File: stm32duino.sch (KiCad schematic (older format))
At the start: 19 parts, among them P1 RF7021SE, P2 DISP_I2C, P3 DISP_SER, P4 HOST_SER, U1 stm32f103c8t6-module-china

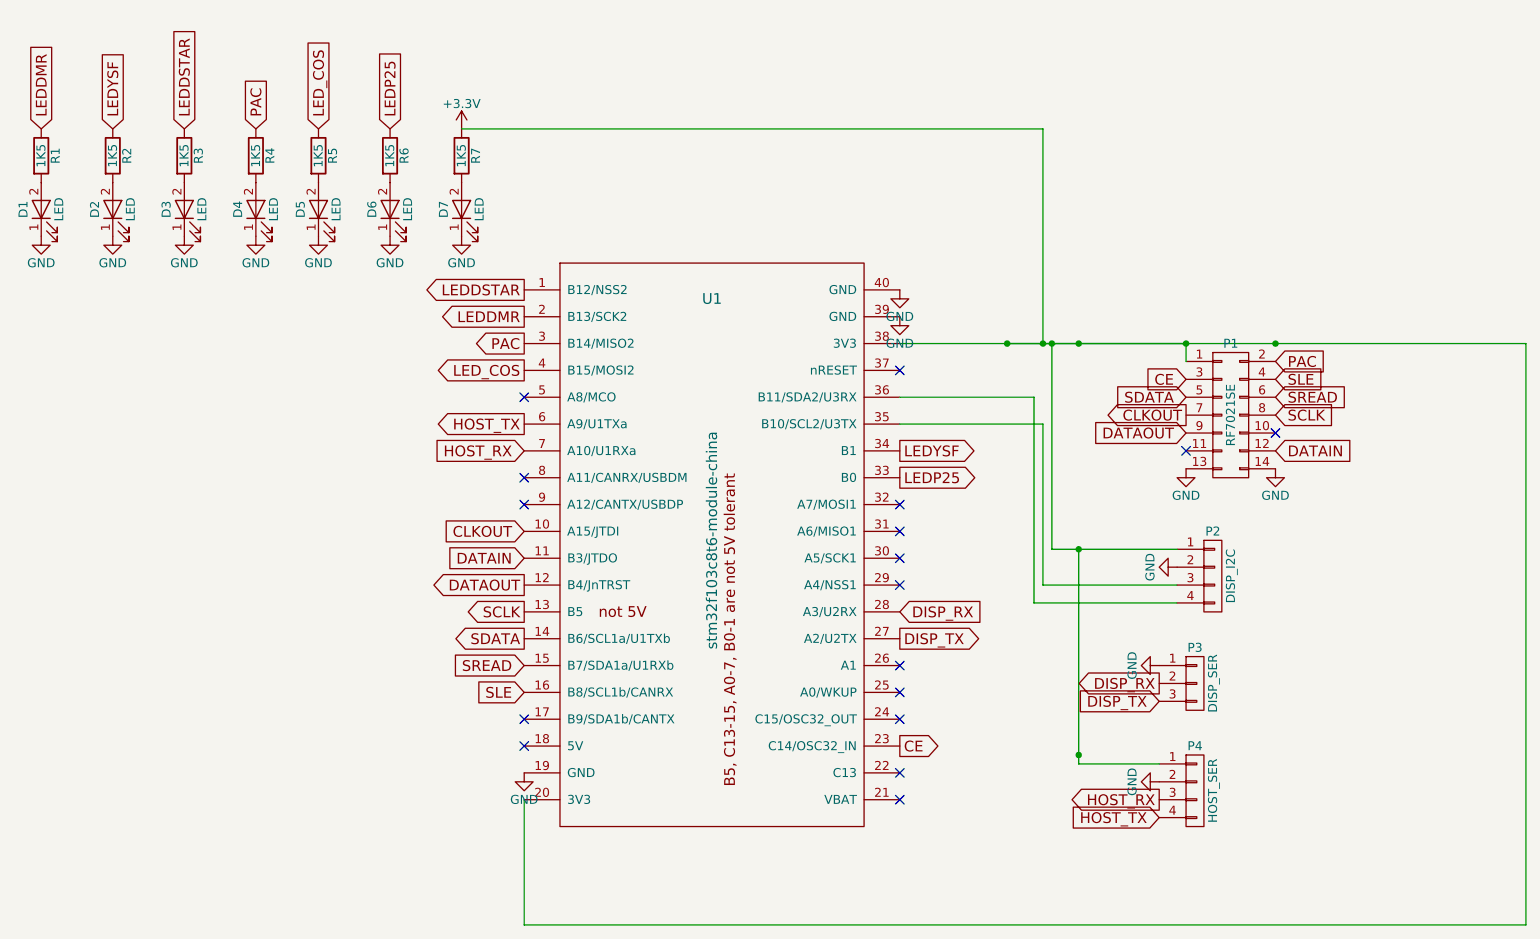
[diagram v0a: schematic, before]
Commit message: Minor beautification, added OSHW logo to PCB
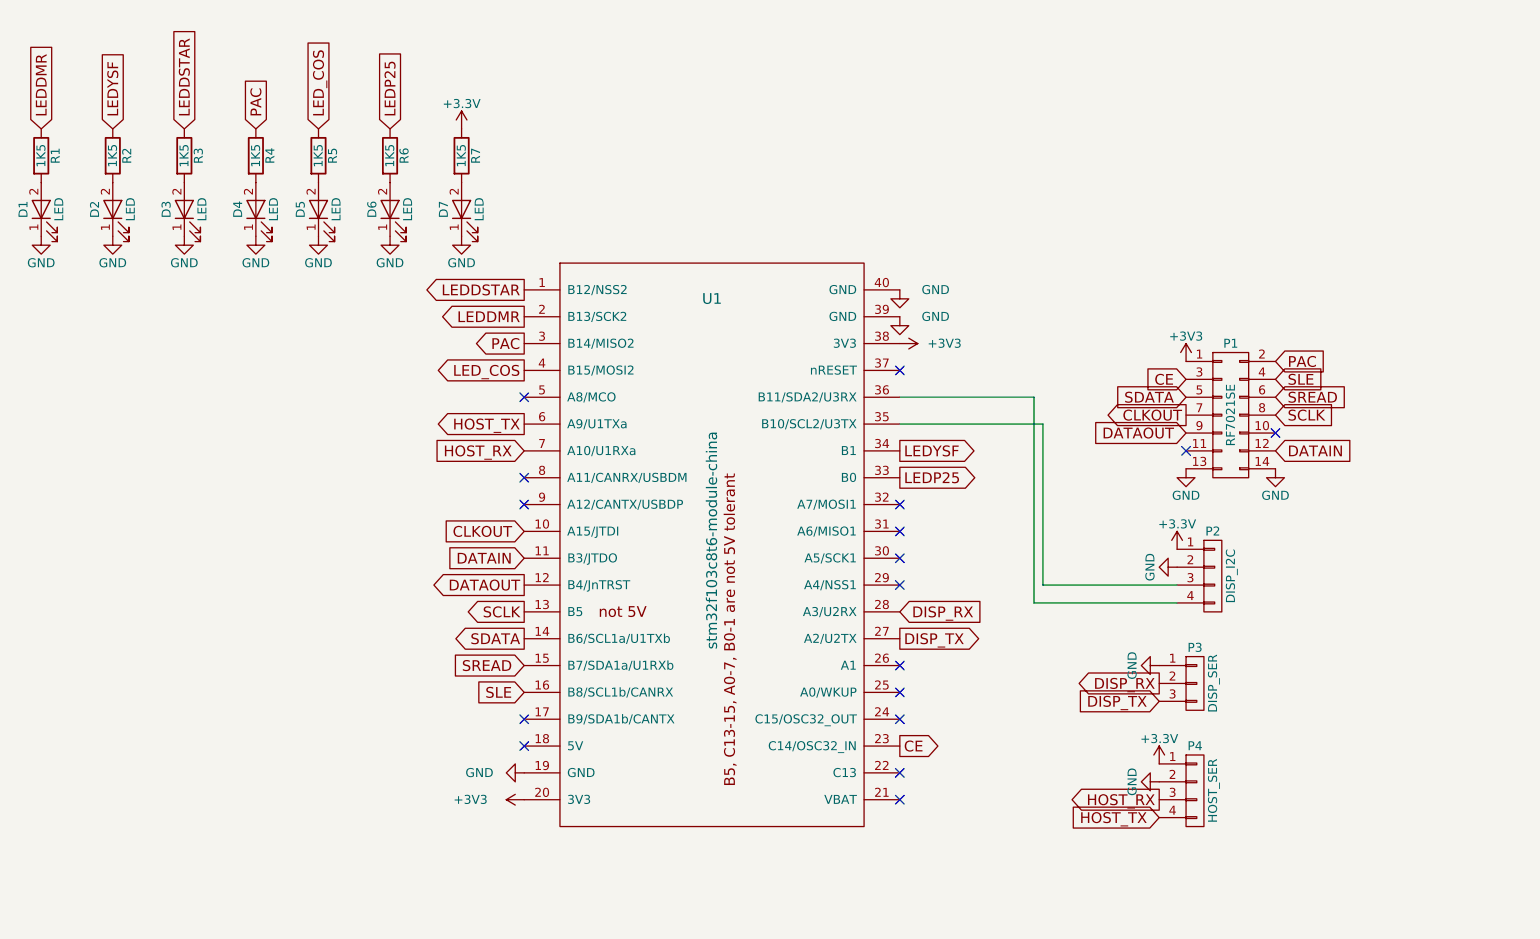
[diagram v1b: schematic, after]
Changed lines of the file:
@@
 P 6200 1900
 F 0 "#PWR10" H 6200 1650 50  0001 C CNN
-F 1 "GND" H 6200 1750 50  0000 C CNN
+F 1 "GND" H 6400 1900 50  0000 C CNN
 F 2 "" H 6200 1900 50  0000 C CNN
 F 3 "" H 6200 1900 50  0000 C CNN
@@
 P 6200 2050
 F 0 "#PWR11" H 6200 1800 50  0001 C CNN
-F 1 "GND" H 6200 1900 50  0000 C CNN
+F 1 "GND" H 6400 2050 50  0000 C CNN
 F 2 "" H 6200 2050 50  0000 C CNN
 F 3 "" H 6200 2050 50  0000 C CNN
@@
 P 4100 4600
 F 0 "#PWR9" H 4100 4350 50  0001 C CNN
-F 1 "GND" H 4100 4450 50  0000 C CNN
+F 1 "GND" V 4100 4350 50  0000 C CNN
 F 2 "" H 4100 4600 50  0000 C CNN
 F 3 "" H 4100 4600 50  0000 C CNN
 	1    4100 4600
-	1    0    0    -1
-$EndComp
-Wire Wire Line
-	6200 2200 9700 2200
-Wire Wire Line
-	3750 1000 7000 1000
-Wire Wire Line
-	7000 1000 7000 2200
-Connection ~ 7000 2200
-Wire Wire Line
-	6800 2200 7800 2200
-Wire Wire Line
-	9700 2200 9700 5450
-Wire Wire Line
-	9700 5450 4100 5450
-Connection ~ 6800 2200
-Wire Wire Line
-	4100 5450 4100 4750
-Connection ~ 8300 2200
-Wire Wire Line
-	7800 2200 7800 2300
-Connection ~ 7800 2200
+	0    1    1    0
+$EndComp
 $Comp
 L CONN_01X04 P2
@@
 $EndComp
 Wire Wire Line
-	7050 2200 7050 3350
-Wire Wire Line
-	7050 3350 7750 3350
-Connection ~ 7050 2200
-Wire Wire Line
 	6200 2650 7000 2650
-Wire Wire Line
-	7000 2650 7000 3550
-Wire Wire Line
-	7000 3550 7750 3550
 Wire Wire Line
 	6200 2500 6950 2500
@@
 	1    0    0    -1
 $EndComp
-Connection ~ 7200 2200
-Wire Wire Line
-	7200 4550 7650 4550
-Wire Wire Line
-	7200 3350 7200 4550
-Connection ~ 7200 4500
-Connection ~ 7200 3350
 Text GLabel 4100 2800 0    60   Input ~ 0
 HOST_RX
@@
 Text GLabel 7650 4200 0    60   Input ~ 0
 DISP_TX
+$Comp
+L +3V3 #PWR?
+U 1 1 58E0F416
+P 7800 2300
+F 0 "#PWR?" H 7800 2150 50  0001 C CNN
+F 1 "+3V3" H 7800 2440 50  0000 C CNN
+F 2 "" H 7800 2300 50  0000 C CNN
+F 3 "" H 7800 2300 50  0000 C CNN
+	1    7800 2300
+	1    0    0    -1
+$EndComp
+$Comp
+L +3V3 #PWR?
+U 1 1 58E0F536
+P 4100 4750
+F 0 "#PWR?" H 4100 4600 50  0001 C CNN
+F 1 "+3V3" V 4100 5050 50  0000 C CNN
+F 2 "" H 4100 4750 50  0000 C CNN
+F 3 "" H 4100 4750 50  0000 C CNN
+	1    4100 4750
+	0    -1   -1   0
+$EndComp
+$Comp
+L +3.3V #PWR?
+U 1 1 58E10142
+P 7750 3350
+F 0 "#PWR?" H 7750 3200 50  0001 C CNN
+F 1 "+3.3V" H 7750 3490 50  0000 C CNN
+F 2 "" H 7750 3350 50  0000 C CNN
+F 3 "" H 7750 3350 50  0000 C CNN
+	1    7750 3350
+	1    0    0    -1
+$EndComp
+Wire Wire Line
+	7000 3550 7750 3550
+Wire Wire Line
+	7000 2650 7000 3550
+$Comp
+L +3.3V #PWR?
+U 1 1 58E117A0
+P 7650 4550
+F 0 "#PWR?" H 7650 4400 50  0001 C CNN
+F 1 "+3.3V" H 7650 4690 50  0000 C CNN
+F 2 "" H 7650 4550 50  0000 C CNN
+F 3 "" H 7650 4550 50  0000 C CNN
+	1    7650 4550
+	1    0    0    -1
+$EndComp
+$Comp
+L +3V3 #PWR?
+U 1 1 58E13D3E
+P 6200 2200
+F 0 "#PWR?" H 6200 2050 50  0001 C CNN
+F 1 "+3V3" V 6200 2450 50  0000 C CNN
+F 2 "" H 6200 2200 50  0000 C CNN
+F 3 "" H 6200 2200 50  0000 C CNN
+	1    6200 2200
+	0    1    1    0
+$EndComp
 $EndSCHEMATC
